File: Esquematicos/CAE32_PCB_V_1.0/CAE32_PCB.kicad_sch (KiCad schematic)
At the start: 2 parts, among them U1 ESP32-S3-WROOM-1, U2 74HC4051

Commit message: Se agregaron archivos .md para dar mas informacion
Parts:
- U2: footprint (none) -> Package_SO:SOIC-16W_5.3x10.2mm_P1.27mm
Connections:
- net sd/asd: now reaches U2.8 (GND)
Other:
- added sheet sd (dfg.kicad_sch)
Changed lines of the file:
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@@
 (kicad_sch (version 20211123) (generator eeschema)
   (paper "A4")
+  (wire (pts (xy 181.61 77.47) (xy 181.61 81.28))
+    (stroke (width 0) (type default) (color 0 0 0 0))
+  )
+  (wire (pts (xy 181.61 81.28) (xy 231.14 81.28))
+    (stroke (width 0) (type default) (color 0 0 0 0))
+  )
+  (wire (pts (xy 231.14 81.28) (xy 231.14 129.54))
+    (stroke (width 0) (type default) (color 0 0 0 0))
+  )
+  (symbol (lib_id "74xx:74HC4051") (at 181.61 62.23 0) (unit 1)
+    (in_bom yes) (on_board yes) (fields_autoplaced)
+    (property "Reference" "U2" (id 0) (at 183.6294 46.99 0)
+      (effects (font (size 1.27 1.27)) (justify left))
+    )
+    (property "Value" "74HC4051" (id 1) (at 183.6294 49.53 0)
+      (effects (font (size 1.27 1.27)) (justify left))
+    )
+    (property "Footprint" "Package_SO:SOIC-16W_5.3x10.2mm_P1.27mm" (id 2) (at 181.61 72.39 0)
+      (effects (font (size 1.27 1.27)) hide)
+    )
+    (property "Datasheet" "http://www.ti.com/lit/ds/symlink/cd74hc4051.pdf" (id 3) (at 181.61 72.39 0)
+      (effects (font (size 1.27 1.27)) hide)
+    )
+    (pin "1")
+    (pin "10")
+    (pin "11")
+    (pin "12")
+    (pin "13")
+    (pin "14")
+    (pin "15")
+    (pin "16")
+    (pin "2")
+    (pin "3")
+    (pin "4")
+    (pin "5")
+    (pin "6")
+    (pin "7")
+    (pin "8")
+    (pin "9")
+  )
   (symbol (lib_id "Espressif:ESP32-S3-WROOM-1") (at 88.9 64.77 0) (unit 1)
     (in_bom yes) (on_board yes) (fields_autoplaced)
@@
     (pin "9")
   )
-  (symbol (lib_id "74xx:74HC4051") (at 229.87 95.25 0) (unit 1)
-    (in_bom yes) (on_board yes) (fields_autoplaced)
-    (property "Reference" "U2" (id 0) (at 231.8894 80.01 0)
-      (effects (font (size 1.27 1.27)) (justify left))
+  (sheet (at 217.17 129.54) (size 53.34 26.67) (fields_autoplaced)
+    (stroke (width 0.1524) (type solid) (color 0 0 0 0))
+    (fill (color 0 0 0 0.0000))
+    (property "Sheet name" "sd" (id 0) (at 217.17 128.8284 0)
+      (effects (font (size 1.27 1.27)) (justify left bottom))
     )
-    (property "Value" "74HC4051" (id 1) (at 231.8894 82.55 0)
-      (effects (font (size 1.27 1.27)) (justify left))
+    (property "Sheet file" "dfg.kicad_sch" (id 1) (at 217.17 156.7946 0)
+      (effects (font (size 1.27 1.27)) (justify left top))
     )
-    (property "Footprint" "" (id 2) (at 229.87 105.41 0)
-      (effects (font (size 1.27 1.27)) hide)
+    (pin "asd" input (at 231.14 129.54 90)
+      (effects (font (size 1.27 1.27)) (justify right))
     )
-    (property "Datasheet" "http://www.ti.com/lit/ds/symlink/cd74hc4051.pdf" (id 3) (at 229.87 105.41 0))
-    (pin "1")
-    (pin "10")
-    (pin "11")
-    (pin "12")
-    (pin "13")
-    (pin "14")
-    (pin "15")
-    (pin "16")
-    (pin "2")
-    (pin "3")
-    (pin "4")
-    (pin "5")
-    (pin "6")
-    (pin "7")
-    (pin "8")
-    (pin "9")
   )
   (sheet_instances
     (path "/" (page "1"))
+    (path "/771da5e1-59fc-4f4a-b782-284ea43f01a6" (page "2"))
   )
   (symbol_instances
+    (path "/771da5e1-59fc-4f4a-b782-284ea43f01a6/aa591cef-7670-4df1-9304-6343bf785257"
+      (reference "#PWR0101") (unit 1) (value "GNDREF") (footprint "")
+    )
     (path "/940d28cf-1686-4379-85c5-75b1a125daa3"
       (reference "U1") (unit 1) (value "ESP32-S3-WROOM-1") (footprint "Espressif:ESP32-S3-WROOM-1")
     )
-    (path "/9fdff095-f654-421b-8c11-bb88c07d5d8f"
-      (reference "U2") (unit 1) (value "74HC4051") (footprint "")
+    (path "/2f09ab82-f3be-4a5a-a6dd-b6d8ba2bb062"
+      (reference "U2") (unit 1) (value "74HC4051") (footprint "Package_SO:SOIC-16W_5.3x10.2mm_P1.27mm")
+    )
+    (path "/771da5e1-59fc-4f4a-b782-284ea43f01a6/9c5a7c59-dc69-4dbc-a743-38a223b99b4f"
+      (reference "U3") (unit 1) (value "74HC4051") (footprint "Package_SO:SOIC-16W_5.3x10.2mm_P1.27mm")
     )
   )

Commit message: Actualización del archivo README
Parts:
- added C1: 10uf, Capacitor_SMD:C_0805_2012Metric, symbol Device:C
- added C2: 10uf, Capacitor_SMD:C_0805_2012Metric, symbol Device:C_Polarized
- added C3: 22uf, Capacitor_SMD:C_0805_2012Metric, symbol Device:C
- added C4, C6: 0.1uf, Capacitor_SMD:C_0805_2012Metric, symbol Device:C
- added C5: 1uf, Capacitor_SMD:C_0805_2012Metric, symbol Device:C
- added D1: USBLC6-2SC6, digikey-footprints:SOT23-6L, symbol dk_TVS-Diodes:USBLC6-2SC6
- added J1: USB_A, Connector_USB:USB_Micro-B_Wuerth_629105150521, symbol Connector:USB_A
- added J2: P_UART, digikey-footprints:PinHeader_1x4_P2.54mm_Drill1.02mm, symbol dk_Rectangular-Connectors-Headers-Male-Pins:0022232041
- added J?: Conn_01x08, symbol Connector_Generic:Conn_01x08
- added R1: 10k, Resistor_SMD:R_0805_2012Metric, symbol Device:R_US
- added R2: 0, Resistor_SMD:R_0805_2012Metric, symbol Device:R_US
- added SW1: RESET, symbol Switch:SW_Push
- added SW2: BOOT, symbol Switch:SW_Push
- added U4: SSP1117, Package_TO_SOT_SMD:SOT-223-3_TabPin2, symbol Regulator_Linear:AP1117-33
- added U5: AD7788BRM, eec:Analog_Devices-AD7788BRM-Level_B, symbol eec:AD7788BRM
- U1: Campo4 (none) -> sdf
- U2: Campo4 (none) -> ffff
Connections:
- net sd/asd: no longer U2.8 (GND)
- net at U2.1 (A4): now also J?.5 (Pin_5)
- net S1: now reaches U2.10 (S1)
- net S1: now also U1.17 (GPIO9/TOUCH9/ADC1_CH8/FSPIHD/SUBSPIHD)
- net S0: now reaches U2.11 (S0)
- net S0: now also U1.18 (GPIO10/TOUCH10/ADC1_CH9/FSPICS0/FSPIIO4/SUBSPICS0)
- net at U2.12 (A3): now also J?.4 (Pin_4)
- net at U2.13 (A0): now also J?.1 (Pin_1)
- net at U2.14 (A1): now also J?.2 (Pin_2)
- net at U2.15 (A2): now also J?.3 (Pin_3)
- net at U2.2 (A6): now also J?.7 (Pin_7)
- net at U2.3 (A): now also U5.3 (AIN(+))
- net at U2.4 (A7): now also J?.8 (Pin_8)
- net at U2.5 (A5): now also J?.6 (Pin_6)
- net S2: now reaches U2.9 (S2)
- net S2: now also U1.12 (GPIO8/TOUCH8/ADC1_CH7/SUBSPICS1)
- net GNDREF: now reaches U1.1 (GND), U1.40 (GND), U1.41 (GND)
- net GNDREF: now also U2.8 (GND), C1.2, C2.2, C3.2, C4.2, C5.1, C6.2, D1.2, J1.4 (GND), J2.4, SW1.2, SW2.2, U4.1 (GND)
- net D-: now reaches U1.13 (GPIO19/U1RTS/ADC2_CH8/CLK_OUT2/USB_D-)
- net D-: now also D1.4
- net D+: now reaches U1.14 (GPIO20/U1CTS/ADC2_CH9/CLK_OUT1/USB_D+)
- net D+: now also D1.6
- net CS_ADC: now reaches U1.19 (GPIO11/TOUCH11/ADC2_CH0/FSPID/FSPIIO5/SUBSPID)
- net CS_ADC: now also U5.2 (~{CS})
- net +3.3V: now reaches U1.2 (3V3)
- net +3.3V: now also C2.1, C3.1, C4.1, J2.1, R1.1, U4.2 (VO)
- net SPICLK: now reaches U1.20 (GPIO12/TOUCH12/ADC2_CH1/FSPICLK/FSPIIO6/SUBSPICLK)
- net SPICLK: now also U5.1 (SCLK)
- net MISO: now reaches U1.21 (GPIO13/TOUCH13/ADC2_CH2/FSPIQ/FSPIIO7/SUBSPIQ)
- net MISO: now also U5.9 (~{RDY})
- net MOSI: now reaches U1.22 (GPIO14/TOUCH14/ADC2_CH3/FSPIWP/FSPIDQS/SUBSPIWP)
- net MOSI: now also U5.10 (DIN)
- net BOOT: now reaches U1.27 (GPIO0/BOOT)
- net BOOT: now also SW2.1
- net EN: now reaches U1.3 (EN)
- net EN: now also C5.2, R1.2, R2.1
- net TX0: now reaches U1.36 (U0RXD/GPIO44/CLK_OUT2)
- net TX0: now also J2.2
- net RX0: now reaches U1.37 (U0TXD/GPIO43/CLK_OUT1)
- net RX0: now also J2.3
- new net: C6.1, R2.2, SW1.1
- new net: D1.3, J1.2 (D-)
- new net: D1.1, J1.3 (D+)
- new net +5V: C1.1, D1.5, J1.1 (VBUS), U4.3 (VI)
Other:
- note added: "ESD protection"
- moved on the sheet: U1, U2

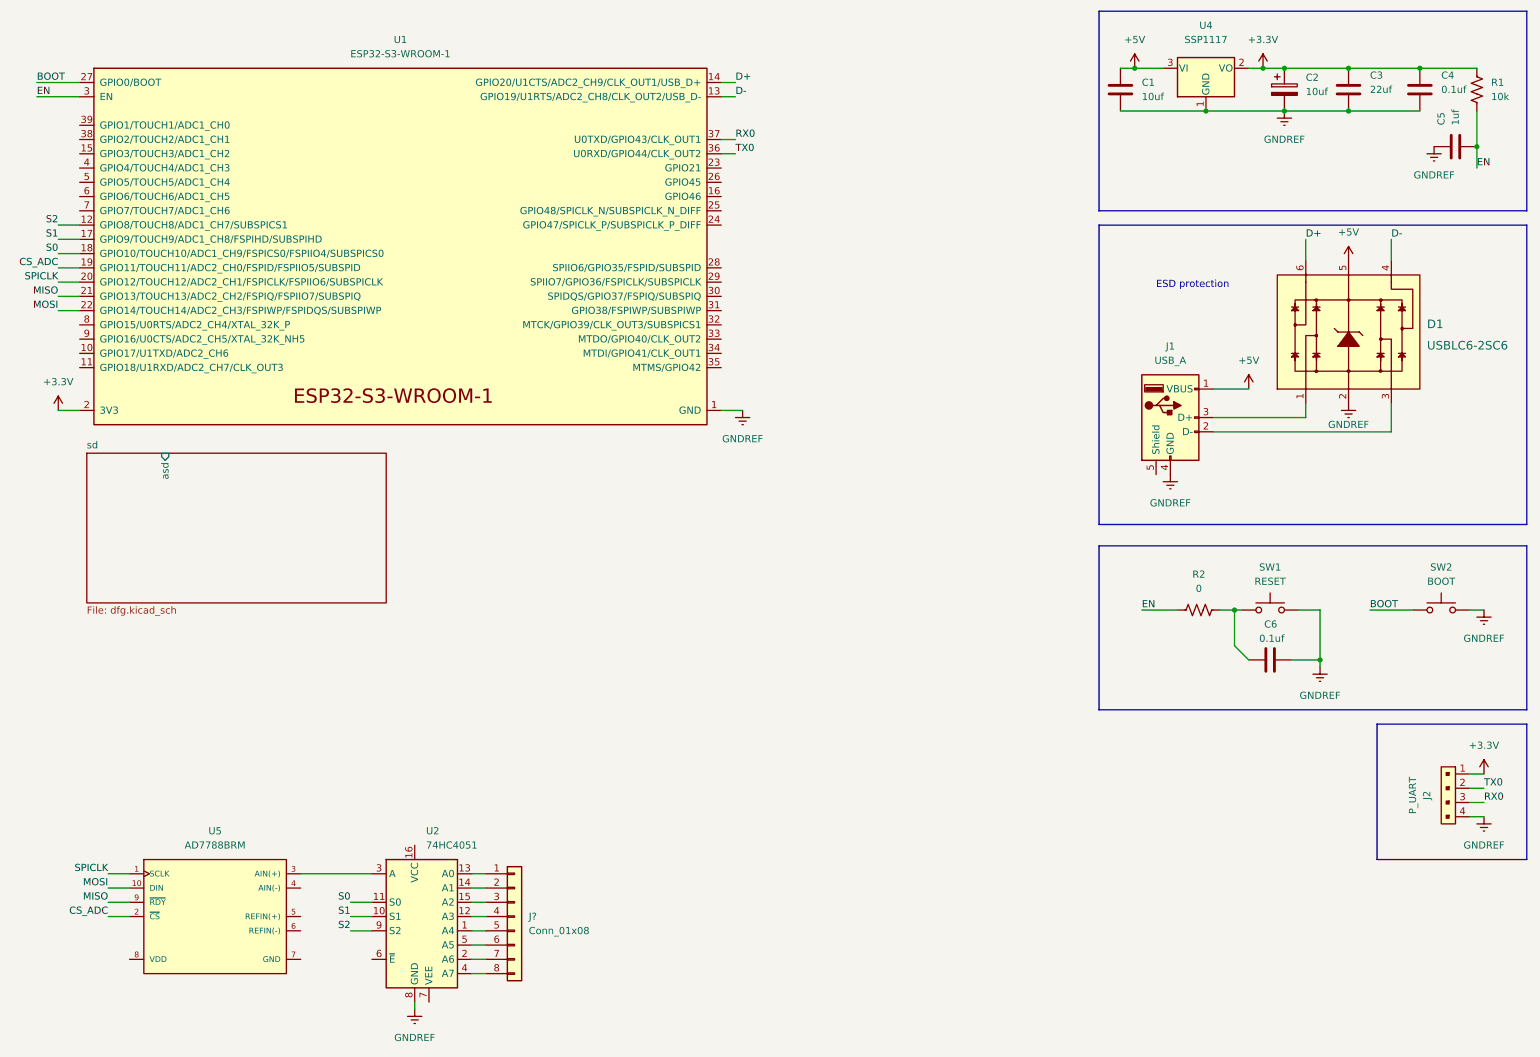
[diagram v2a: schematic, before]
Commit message: Detección de dispositivos (Joystick, HID)
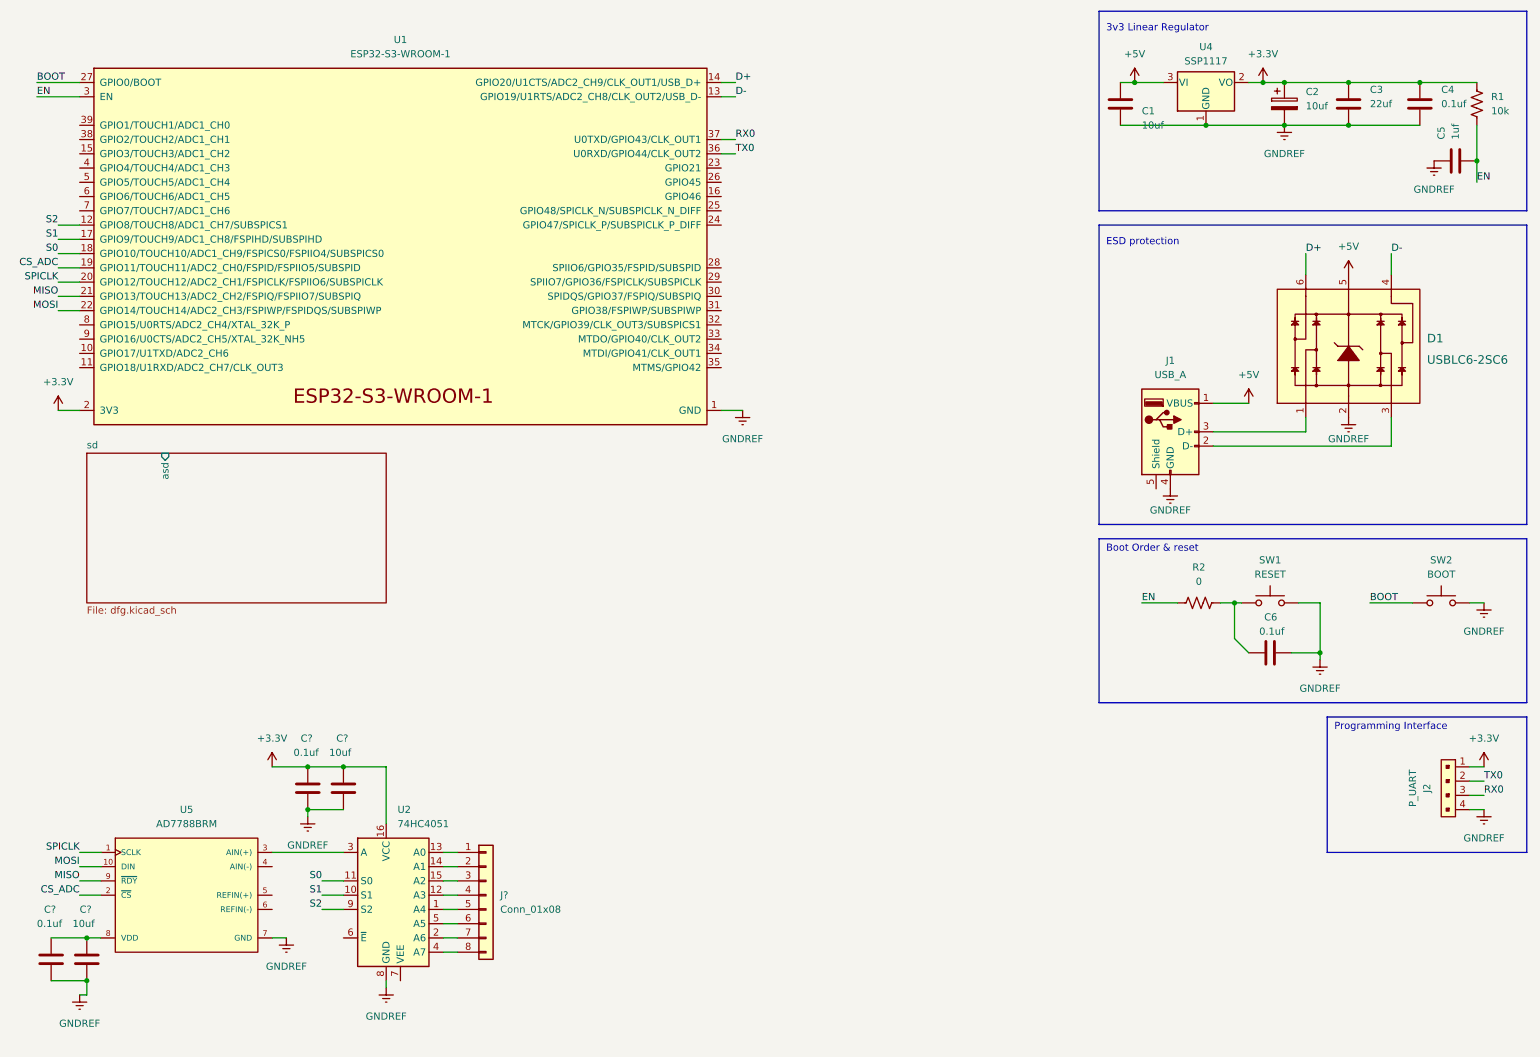
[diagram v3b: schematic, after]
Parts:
- added C? (x2): 0.1uf, Capacitor_SMD:C_0805_2012Metric, symbol Device:C
- added C? (x2): 10uf, Capacitor_SMD:C_0805_2012Metric, symbol Device:C
- U5: Campo4 (none) -> https://datasheet.lcsc.com/lcsc/2006191006_Analog-Devices-A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
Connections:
- net +3.3V: now also U2.16 (VCC), C?.1, C?.1
- net GNDREF: now also U5.7 (GND), C?.2, C?.2, C?.2, C?.2
- net at U5.8 (VDD): now also C?.1, C?.1
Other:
- note added: "3v3 Linear Regulator"
- note added: "Boot Order & reset"
- note added: "Programming Interface"
- moved on the sheet: C1, C2, C3, C4, C5, C6, D1, J1, J2, J?, R1, R2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
